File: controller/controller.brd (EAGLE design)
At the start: 51.7 x 71.1 mm, 26 parts, among them IC1 ATtiny25, IC2 74HC595N

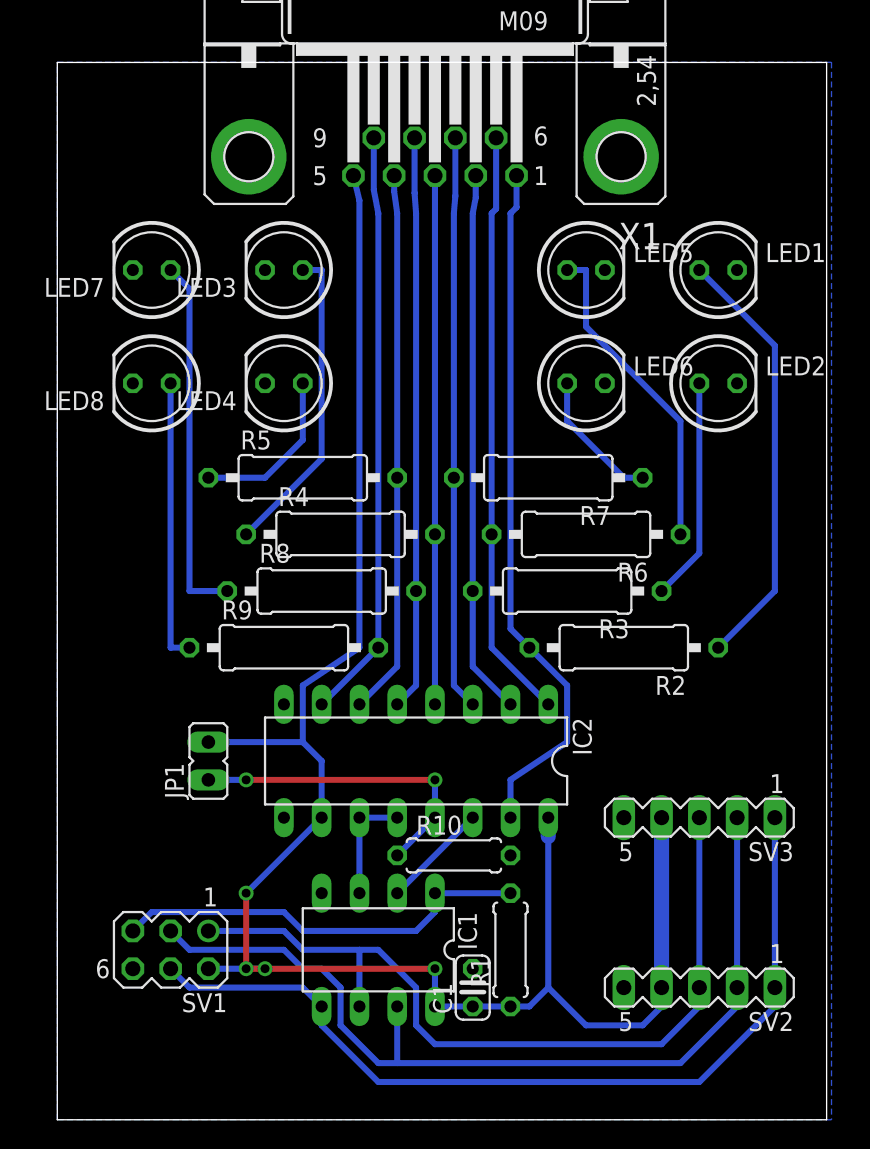
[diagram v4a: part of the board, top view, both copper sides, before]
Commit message: Mehr Abstand in der GND-Isolation
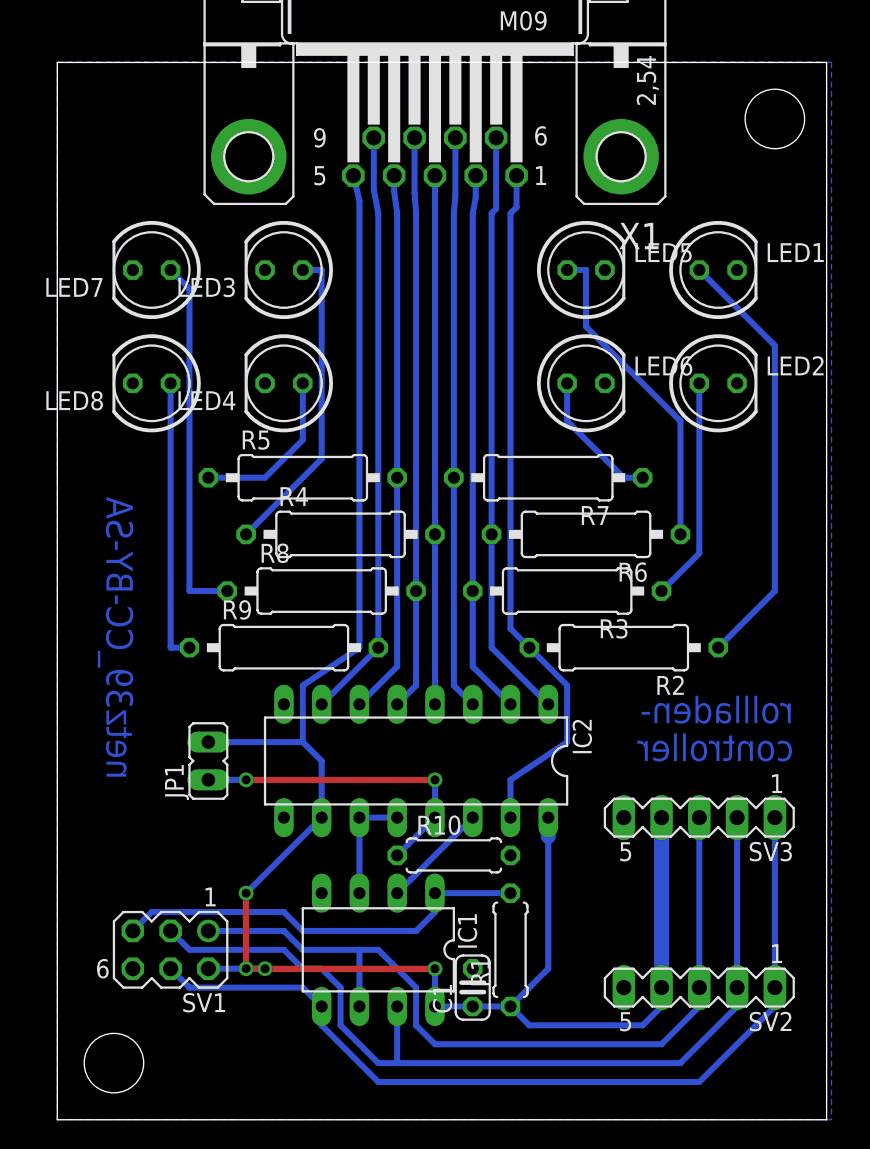
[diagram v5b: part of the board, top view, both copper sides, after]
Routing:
- net VCC: track 124.9 -> 126.2 mm
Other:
- board text added: "controller"
- board text added: "netz39_CC-BY-SA"
- board text added: "rollladen-"
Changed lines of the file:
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@@
 <setting verticaltext="up"/>
 </settings>
-<grid distance="0.05" unitdist="inch" unit="inch" style="lines" multiple="1" display="no" altdistance="0.025" altunitdist="inch" altunit="inch"/>
+<grid distance="1.27" unitdist="mm" unit="mm" style="lines" multiple="1" display="no" altdistance="0.025" altunitdist="inch" altunit="inch"/>
 <layers>
 <layer number="1" name="Top" color="4" fill="1" visible="yes" active="yes"/>
@@
 <layer number="20" name="Dimension" color="15" fill="1" visible="yes" active="yes"/>
 <layer number="21" name="tPlace" color="7" fill="1" visible="yes" active="yes"/>
-<layer number="22" name="bPlace" color="7" fill="1" visible="yes" active="yes"/>
-<layer number="23" name="tOrigins" color="15" fill="1" visible="yes" active="yes"/>
-<layer number="24" name="bOrigins" color="15" fill="1" visible="yes" active="yes"/>
+<layer number="22" name="bPlace" color="7" fill="1" visible="no" active="yes"/>
+<layer number="23" name="tOrigins" color="15" fill="1" visible="no" active="yes"/>
+<layer number="24" name="bOrigins" color="15" fill="1" visible="no" active="yes"/>
 <layer number="25" name="tNames" color="7" fill="1" visible="yes" active="yes"/>
-<layer number="26" name="bNames" color="7" fill="1" visible="yes" active="yes"/>
+<layer number="26" name="bNames" color="7" fill="1" visible="no" active="yes"/>
 <layer number="27" name="tValues" color="7" fill="1" visible="yes" active="yes"/>
-<layer number="28" name="bValues" color="7" fill="1" visible="yes" active="yes"/>
+<layer number="28" name="bValues" color="7" fill="1" visible="no" active="yes"/>
 <layer number="29" name="tStop" color="7" fill="3" visible="no" active="yes"/>
 <layer number="30" name="bStop" color="7" fill="6" visible="no" active="yes"/>
@@
 <layer number="37" name="tTest" color="7" fill="1" visible="no" active="yes"/>
 <layer number="38" name="bTest" color="7" fill="1" visible="no" active="yes"/>
-<layer number="39" name="tKeepout" color="4" fill="11" visible="yes" active="yes"/>
-<layer number="40" name="bKeepout" color="1" fill="11" visible="yes" active="yes"/>
-<layer number="41" name="tRestrict" color="4" fill="10" visible="yes" active="yes"/>
-<layer number="42" name="bRestrict" color="1" fill="10" visible="yes" active="yes"/>
-<layer number="43" name="vRestrict" color="2" fill="10" visible="yes" active="yes"/>
+<layer number="39" name="tKeepout" color="4" fill="11" visible="no" active="yes"/>
+<layer number="40" name="bKeepout" color="1" fill="11" visible="no" active="yes"/>
+<layer number="41" name="tRestrict" color="4" fill="10" visible="no" active="yes"/>
+<layer number="42" name="bRestrict" color="1" fill="10" visible="no" active="yes"/>
+<layer number="43" name="vRestrict" color="2" fill="10" visible="no" active="yes"/>
 <layer number="44" name="Drills" color="7" fill="1" visible="no" active="yes"/>
 <layer number="45" name="Holes" color="7" fill="1" visible="no" active="yes"/>
 <layer number="46" name="Milling" color="3" fill="1" visible="no" active="yes"/>
 <layer number="47" name="Measures" color="7" fill="1" visible="no" active="yes"/>
-<layer number="48" name="Document" color="7" fill="1" visible="yes" active="yes"/>
-<layer number="49" name="Reference" color="7" fill="1" visible="yes" active="yes"/>
+<layer number="48" name="Document" color="7" fill="1" visible="no" active="yes"/>
+<layer number="49" name="Reference" color="7" fill="1" visible="no" active="yes"/>
 <layer number="50" name="dxf" color="7" fill="1" visible="no" active="no"/>
 <layer number="51" name="tDocu" color="7" fill="1" visible="yes" active="yes"/>
-<layer number="52" name="bDocu" color="7" fill="1" visible="yes" active="yes"/>
+<layer number="52" name="bDocu" color="7" fill="1" visible="no" active="yes"/>
 <layer number="91" name="Nets" color="2" fill="1" visible="no" active="no"/>
 <layer number="92" name="Busses" color="1" fill="1" visible="no" active="no"/>
@@
 <wire x1="51.74" y1="71.11" x2="0" y2="71.11" width="0" layer="20"/>
 <wire x1="0" y1="71.11" x2="0" y2="0" width="0" layer="20"/>
+<text x="5.08" y="41.91" size="1.778" layer="16" font="vector" rot="MR270">netz39_CC-BY-SA</text>
+<text x="49.53" y="26.67" size="1.778" layer="16" font="vector" rot="MR0">rollladen-</text>
+<text x="49.53" y="24.13" size="1.778" layer="16" font="vector" rot="MR0">controller</text>
+<hole x="3.81" y="3.81" drill="4"/>
+<hole x="48.26" y="67.31" drill="4"/>
 </plain>
 <attributes>
@@
 <contactref element="X1" pad="G1"/>
 <contactref element="X1" pad="G2"/>
-<polygon width="0.4064" layer="16" isolate="0.254">
+<polygon width="0.4064" layer="16" isolate="0.4064">
 <vertex x="0" y="71.12"/>
 <vertex x="52.07" y="71.12"/>
@@
 <wire x1="20.32" y1="31.75" x2="20.32" y2="61.8236" width="0.4064" layer="16"/>
 <wire x1="40.64" y1="20.32" x2="40.64" y2="8.89" width="1.016" layer="16"/>
-<via x="25.4" y="10.16" extent="1-16" drill="0.6" diameter="0.6096"/>
-<via x="13.97" y="10.16" extent="1-16" drill="0.6" diameter="0.6096"/>
-<via x="12.7" y="15.24" extent="1-16" drill="0.6" diameter="0.6096"/>
+<via x="25.4" y="10.16" extent="1-16" drill="0.6" diameter="0.8128"/>
+<via x="13.97" y="10.16" extent="1-16" drill="0.6" diameter="0.8128"/>
+<via x="12.7" y="15.24" extent="1-16" drill="0.6" diameter="0.8128"/>
 <wire x1="25.4" y1="7.62" x2="25.4" y2="10.16" width="0.4064" layer="16"/>
 <wire x1="25.4" y1="10.16" x2="13.97" y2="10.16" width="0.4064" layer="1"/>
@@
 <wire x1="33.02" y1="20.32" x2="33.02" y2="19.05" width="1.016" layer="16"/>
 <wire x1="27.94" y1="7.62" x2="30.48" y2="7.62" width="0.4064" layer="16"/>
-<wire x1="30.48" y1="7.62" x2="31.75" y2="7.62" width="0.4064" layer="16"/>
-<wire x1="31.75" y1="7.62" x2="33.02" y2="8.89" width="0.4064" layer="16"/>
-<wire x1="33.02" y1="8.89" x2="33.02" y2="19.05" width="0.4064" layer="16"/>
+<wire x1="30.48" y1="7.62" x2="33.02" y2="10.16" width="0.4064" layer="16"/>
+<wire x1="33.02" y1="10.16" x2="33.02" y2="19.05" width="0.4064" layer="16"/>
 <wire x1="40.64" y1="8.89" x2="40.64" y2="7.62" width="0.4064" layer="16"/>
 <wire x1="40.64" y1="7.62" x2="39.37" y2="6.35" width="0.4064" layer="16"/>
-<wire x1="39.37" y1="6.35" x2="35.56" y2="6.35" width="0.4064" layer="16"/>
-<wire x1="35.56" y1="6.35" x2="33.02" y2="8.89" width="0.4064" layer="16"/>
+<wire x1="39.37" y1="6.35" x2="31.75" y2="6.35" width="0.4064" layer="16"/>
+<wire x1="31.75" y1="6.35" x2="30.48" y2="7.62" width="0.4064" layer="16"/>
 </signal>
 <signal name="RESET">
@@
 </signal>
 <signal name="N$13">
-<via x="12.7" y="10.16" extent="1-16" drill="0.6" diameter="0.6096"/>
+<via x="12.7" y="10.16" extent="1-16" drill="0.6" diameter="0.8128"/>
 </signal>
 <signal name="REG_DISABLE">

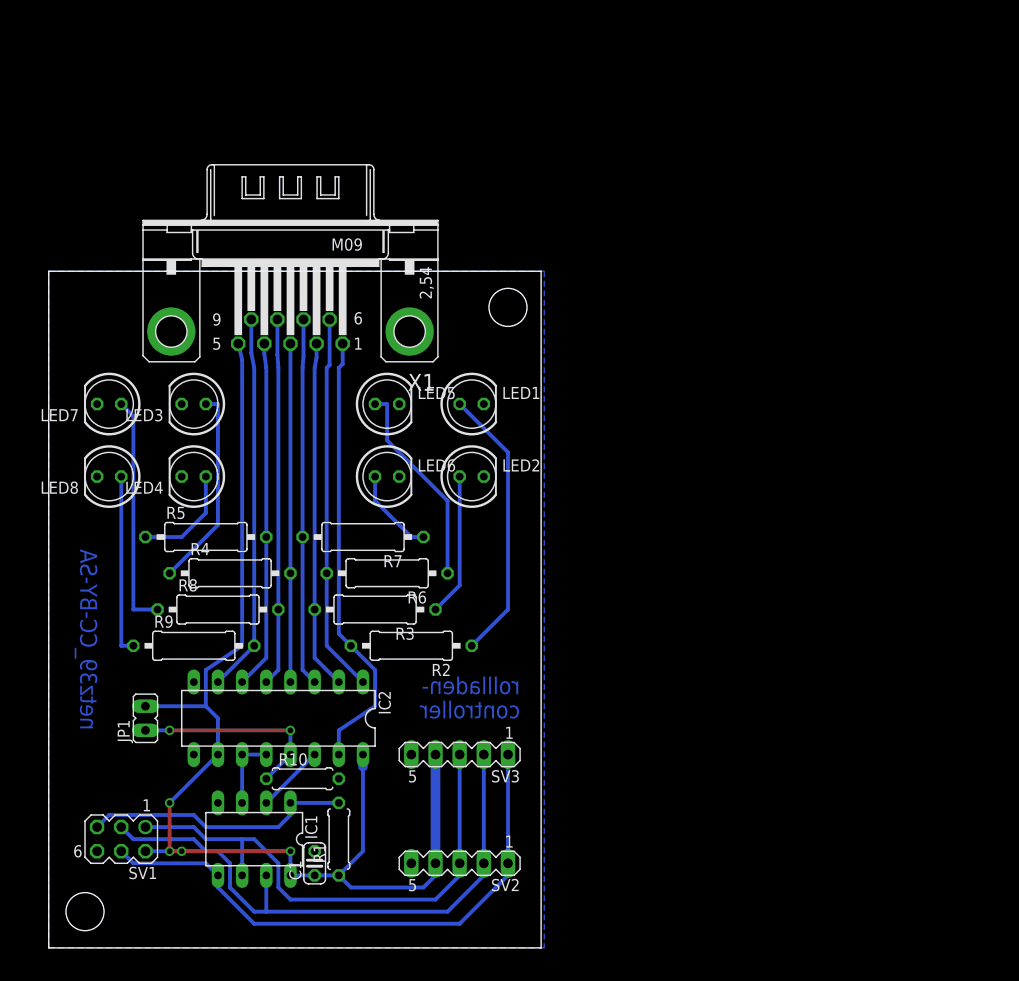
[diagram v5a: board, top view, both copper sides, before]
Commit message: * Platinenlayout nochmal angepasst (hauptsächlich Leiterbahndicken) * dritten Bus-Stecker vorgesehen
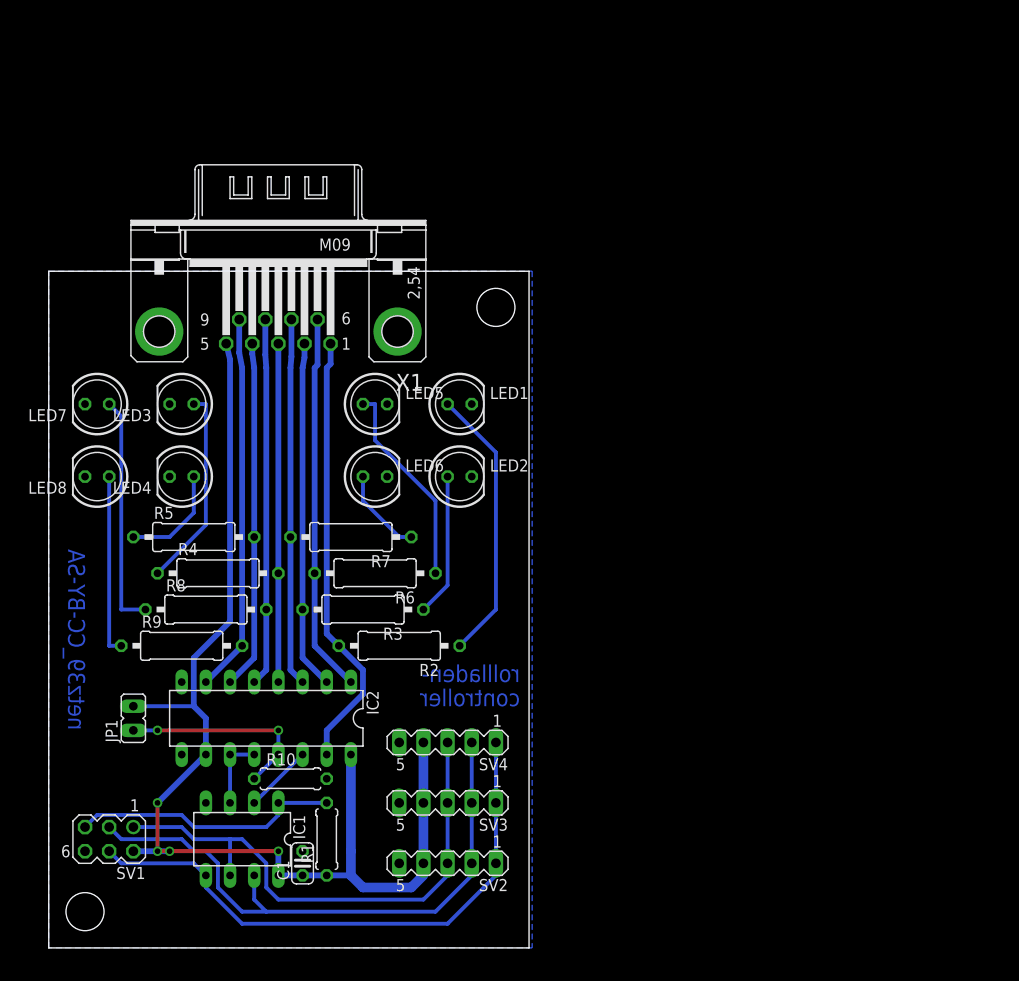
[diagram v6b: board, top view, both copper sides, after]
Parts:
- added SV4: (no value), con-lstb:MA05-1
- moved SV3 5.24 mm to (41.9, 15.2)
- moved LED1 1.27 mm to (43.2, 57.1)
- moved LED2 1.27 mm to (43.2, 49.5)
- moved LED5 1.27 mm to (34.3, 57.1)
- moved LED6 1.27 mm to (34.3, 49.5)
- moved R10 1.27 mm to (25.4, 17.8)
- moved R2 1.27 mm to (36.8, 31.8)
- moved R6 1.27 mm to (34.3, 39.4)
- moved R7 1.27 mm to (31.8, 43.2)
- moved SV2 1.27 mm to (41.9, 8.89)
- moved R5 1.27 mm to (15.2, 43.2)
- moved SV1 1.27 mm to (6.35, 11.4)
- moved C1 1.27 mm to (26.7, 8.89)
- moved IC1 1.27 mm to (20.3, 11.4)
- moved IC2 1.27 mm to (22.9, 24.1)
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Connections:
- net GND: now also SV4.5
- net MISO: now also SV4.3
- net MOSI: now also SV4.1
- net SCK: now also SV4.2
- net VCC: now also SV4.4
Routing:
- net MOSI: track 59.3 -> 60.6 mm
- net SCK: track 61.4 -> 61.9 mm
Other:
- board size 51.7 x 71.1 mm -> 50.5 x 71.1 mm
